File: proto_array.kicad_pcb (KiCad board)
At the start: 2 copper layers, 99.1 x 129.5 mm, 60 parts, among them P1 CONN_01X03, P2 CONN_01X03, P3 CONN_01X03, P4 CONN_01X03, P5 CONN_01X03, U1 ADS131E08, U2 BEAGLEBONEBLACK

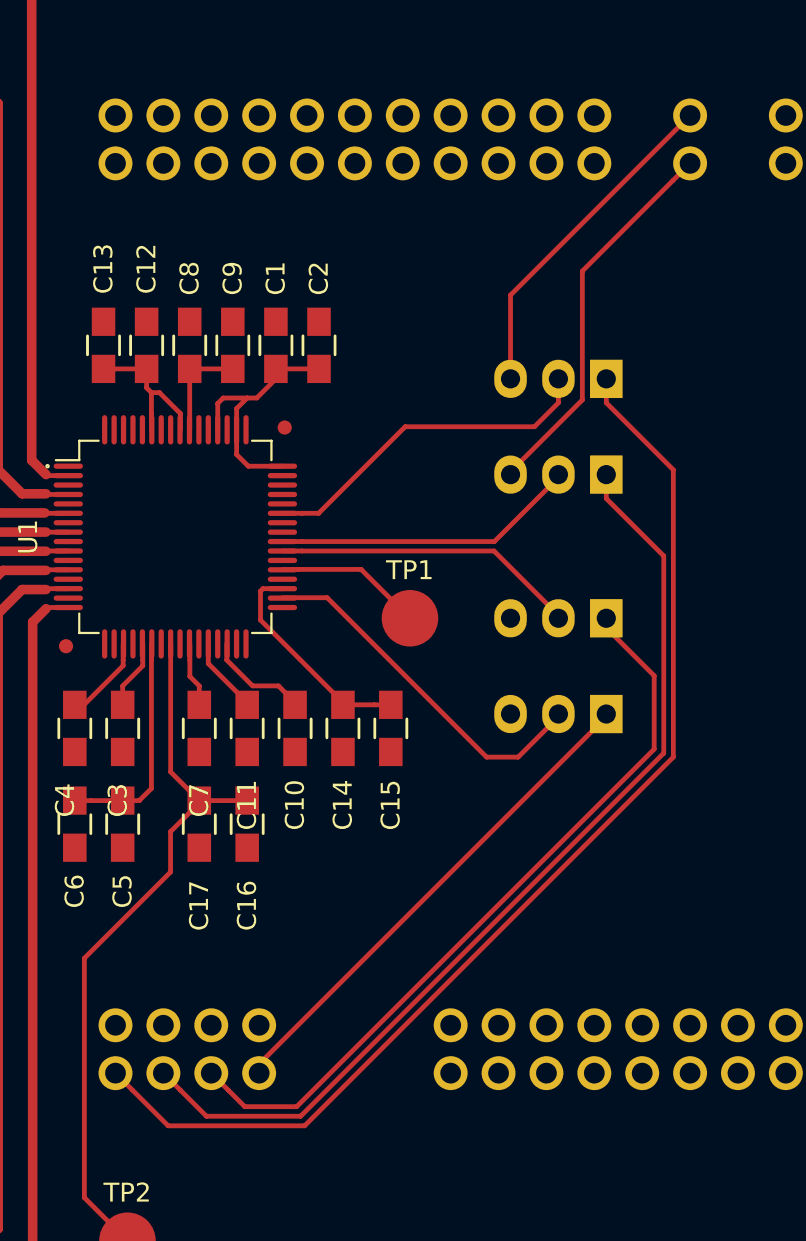
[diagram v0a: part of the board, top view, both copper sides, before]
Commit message: Eliminated the headers for SPI interface to make PCB single layer.
Signed-off-by: Chamon <[luizchamon@gmail.com>
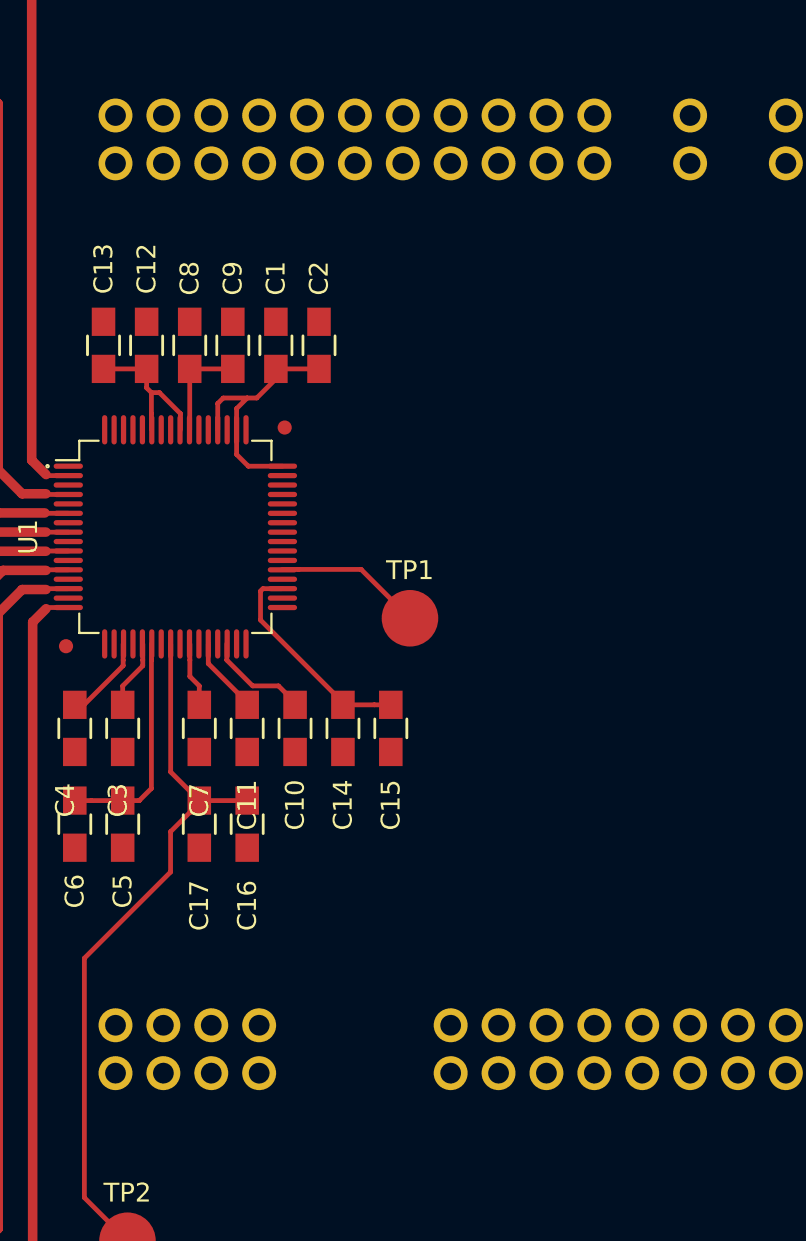
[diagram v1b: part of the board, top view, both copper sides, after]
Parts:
- removed P2, P3, P4, P5: CONN_01X03, Pin_Headers:Pin_Header_Straight_1x03
- moved P1 39.9 mm to (101.6, 49.5)
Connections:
- P1 pad 1: /PRU1_5 -> /BBB_VDD_5V
- P1 pad 2: Net-(P1-Pad2) -> AVDD
- P1 pad 3: /SPI0_CS -> /BBB_SYS_5V
- U1 pad 34: Net-(P3-Pad2) -> /PRU1_7
- U1 pad 39: Net-(P1-Pad2) -> /PRU1_5
- U1 pad 40: Net-(P2-Pad2) -> /PRU1_3
- U1 pad 43: Net-(P4-Pad2) -> /PRU1_1
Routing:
- net /PRU1_1: track 60.4 -> 0.00 mm
- net /PRU1_3: track 51.5 -> 0.00 mm
- net /PRU1_5: track 40.1 -> 0.00 mm
- net /PRU1_7: track 26.7 -> 0.48 mm
- net /SPI0_CLK: track 20.5 -> 0.00 mm
- net Net-(P3-Pad2): track 19.2 -> 0.00 mm
- net Net-(P4-Pad2): track 18.3 -> 0.00 mm
- net /SPI0_MISO: track 17.9 -> 0.00 mm
- net Net-(P1-Pad2): track 16.2 -> 0.00 mm
- net Net-(P2-Pad2): track 16.2 -> 0.00 mm

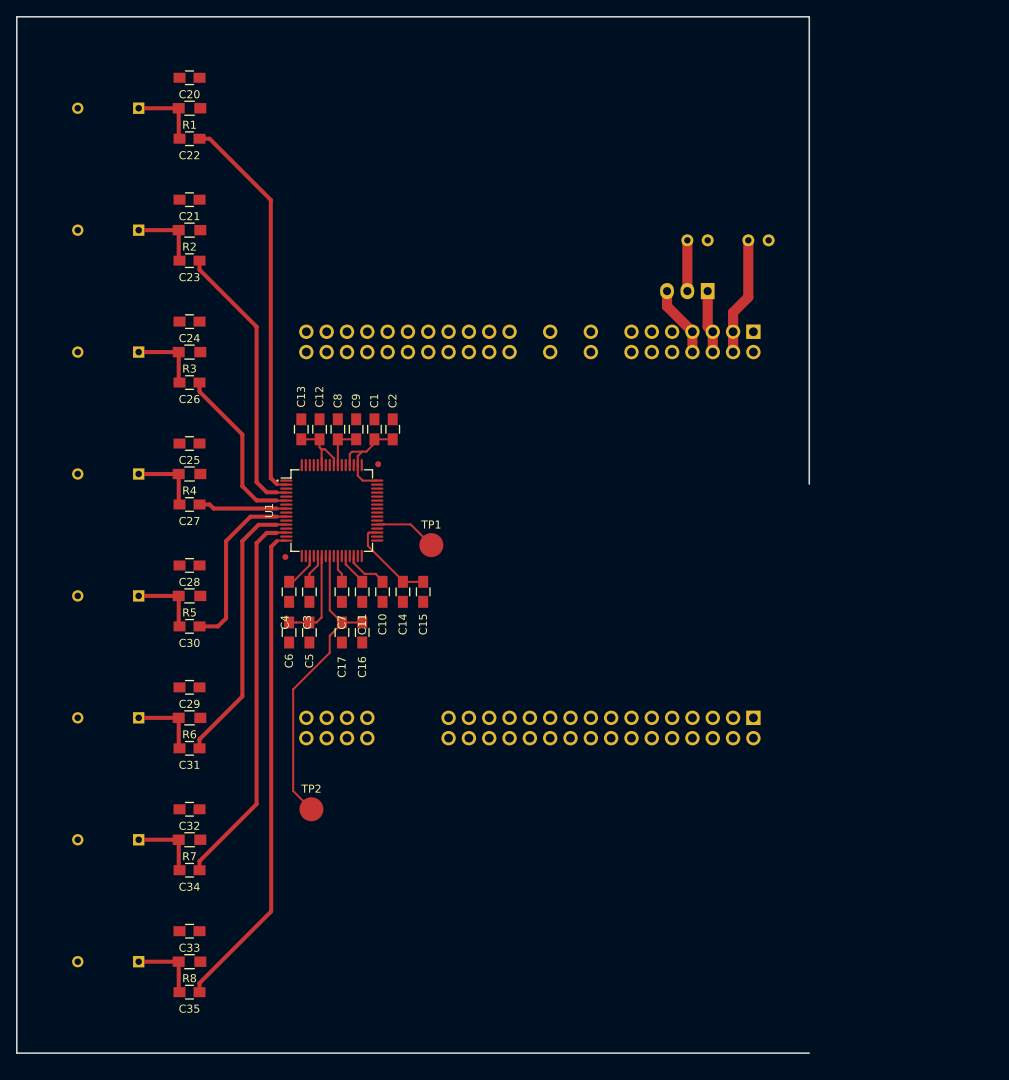
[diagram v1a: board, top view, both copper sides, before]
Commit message: Routed AVDD. Trying to solve ground routing.
Signed-off-by: Chamon <[luizchamon@gmail.com>
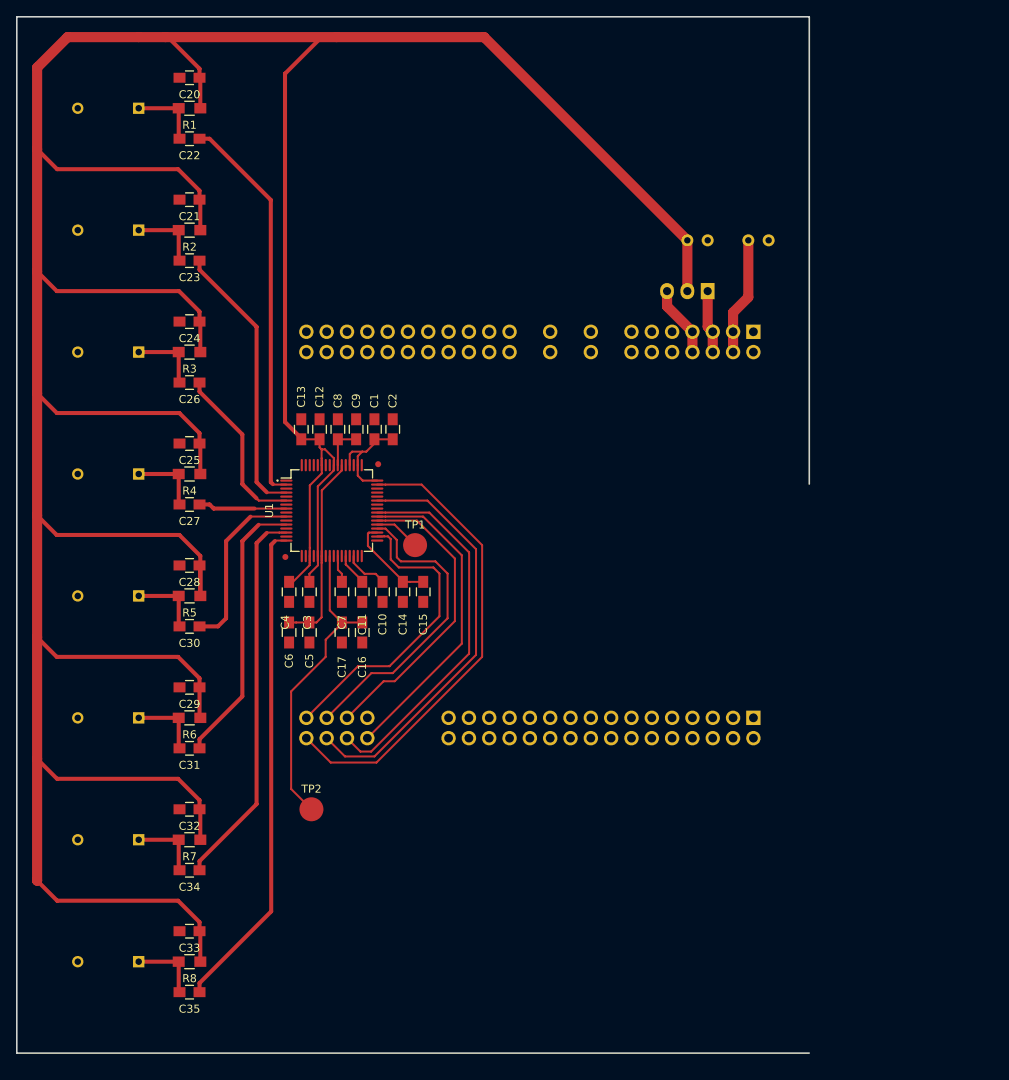
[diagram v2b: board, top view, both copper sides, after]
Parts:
- moved TP1 2.03 mm to (65.0, 81.3)
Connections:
- U1 pad 34: /PRU1_7 -> /PRU1_0
- U1 pad 36: /PRU1_4 -> /PRU1_2
- U1 pad 38: /PRU1_0 -> /PRU1_4
- U1 pad 39: /PRU1_5 -> /PRU1_7
- U1 pad 40: /PRU1_3 -> /PRU1_5
- U1 pad 43: /PRU1_1 -> /PRU1_3
- U1 pad 47: /PRU1_2 -> /PRU1_1
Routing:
- net AVDD: track 35.2 -> 528.6 mm
- net /PRU1_1: track 0.00 -> 58.9 mm
- net /PRU1_3: track 0.00 -> 53.0 mm
- net /PRU1_5: track 0.00 -> 47.2 mm
- net /PRU1_7: track 0.48 -> 40.3 mm
- net /PRU1_0: track 0.00 -> 38.4 mm
- net /PRU1_2: track 0.00 -> 38.3 mm
- net /PRU1_4: track 0.00 -> 38.0 mm
- net Net-(TP1-Pad1): track 7.84 -> 5.80 mm

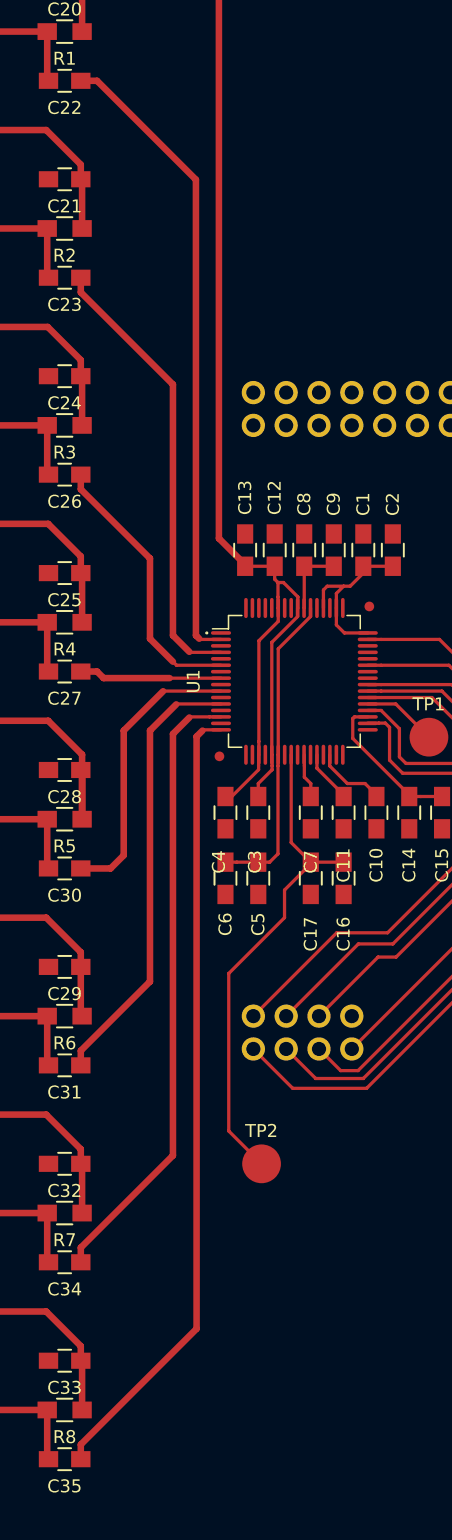
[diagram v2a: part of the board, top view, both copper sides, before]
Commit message: * Fix PRU connections on the schematic * Reduce microphone tracks to fit ground plane * Remove fiducials from ADC IC
Signed-off-by: Chamon <[luizchamon@gmail.com>
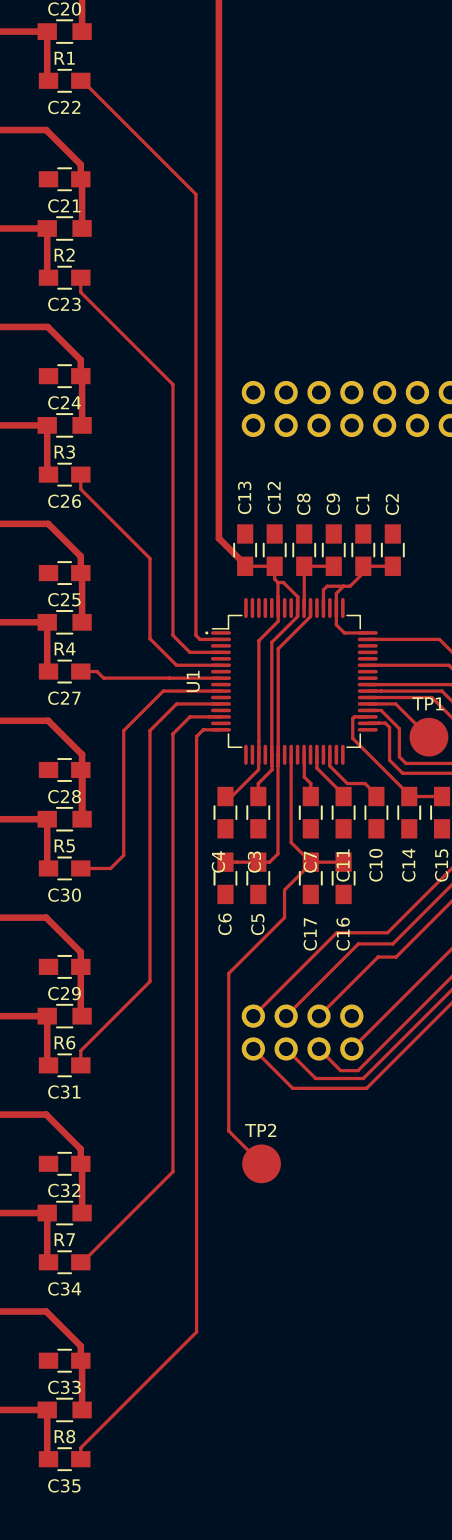
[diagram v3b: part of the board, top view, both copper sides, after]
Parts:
- U1: footprint micarray:LQFP-64_12x12_Pitch0.5mm -> micarray:LQFP-64_12x12_Pitch0.5mm_NoFid
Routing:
- net /MIC_1: track 49.4 -> 48.8 mm

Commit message: Final PCB with one airwire.
Signed-off-by: Chamon <[luizchamon@gmail.com>
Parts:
- removed TP2: TESTPOINT, Measurement_Points:Measurement_Point_Round-SMD-Pad_Big
- moved C14 31.8 mm to (88.9, 68.1), turned to 90 degrees
- moved C15 31.7 mm to (91.4, 68.1), turned to 90 degrees
- moved C19 27.4 mm to (79.5, 47.0), turned to 180 degrees
- moved TP1 24.9 mm to (89.9, 81.8)
- moved C2 24.2 mm to (86.4, 68.1)
- moved C1 23.9 mm to (83.8, 68.1)
- moved C8 23.1 mm to (78.5, 66.8), turned to 180 degrees
- moved U2 22.9 mm to (106.7, 81.3)
- moved C11 22.9 mm to (81.3, 88.4)
- moved C16 22.9 mm to (81.3, 93.5)
- moved C18 22.9 mm to (121.9, 44.5)
- moved C20 22.9 mm to (59.7, 24.1)
- moved C21 22.9 mm to (59.7, 39.4)
- moved C22 22.9 mm to (59.7, 31.8)
- moved C23 22.9 mm to (59.7, 47.0)
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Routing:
- net DVDD: track 40.3 -> 110.3 mm
- net /VREFP: track 38.5 -> 11.5 mm
- net AGND: track 0.00 -> 21.7 mm
- net AVDD: track 528.6 -> 537.4 mm
- net /PRU1_4: track 38.0 -> 44.3 mm
- net /PRU1_0: track 38.4 -> 42.8 mm
- net /PRU1_7: track 40.3 -> 44.7 mm
- net /PRU1_2: track 38.3 -> 42.5 mm
- net /PRU1_5: track 47.2 -> 50.5 mm
- net /PRU1_3: track 53.0 -> 56.2 mm
- net /PRU1_1: track 58.9 -> 62.1 mm
- net Net-(TP1-Pad1): track 5.80 -> 7.52 mm
- net Net-(C8-Pad1): track 5.52 -> 6.47 mm
- added copper zone on F.Cu, net AGND
- added copper zone on F.Cu, net DVDD
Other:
- board text added: "An airwire is required between the digital ground pours."

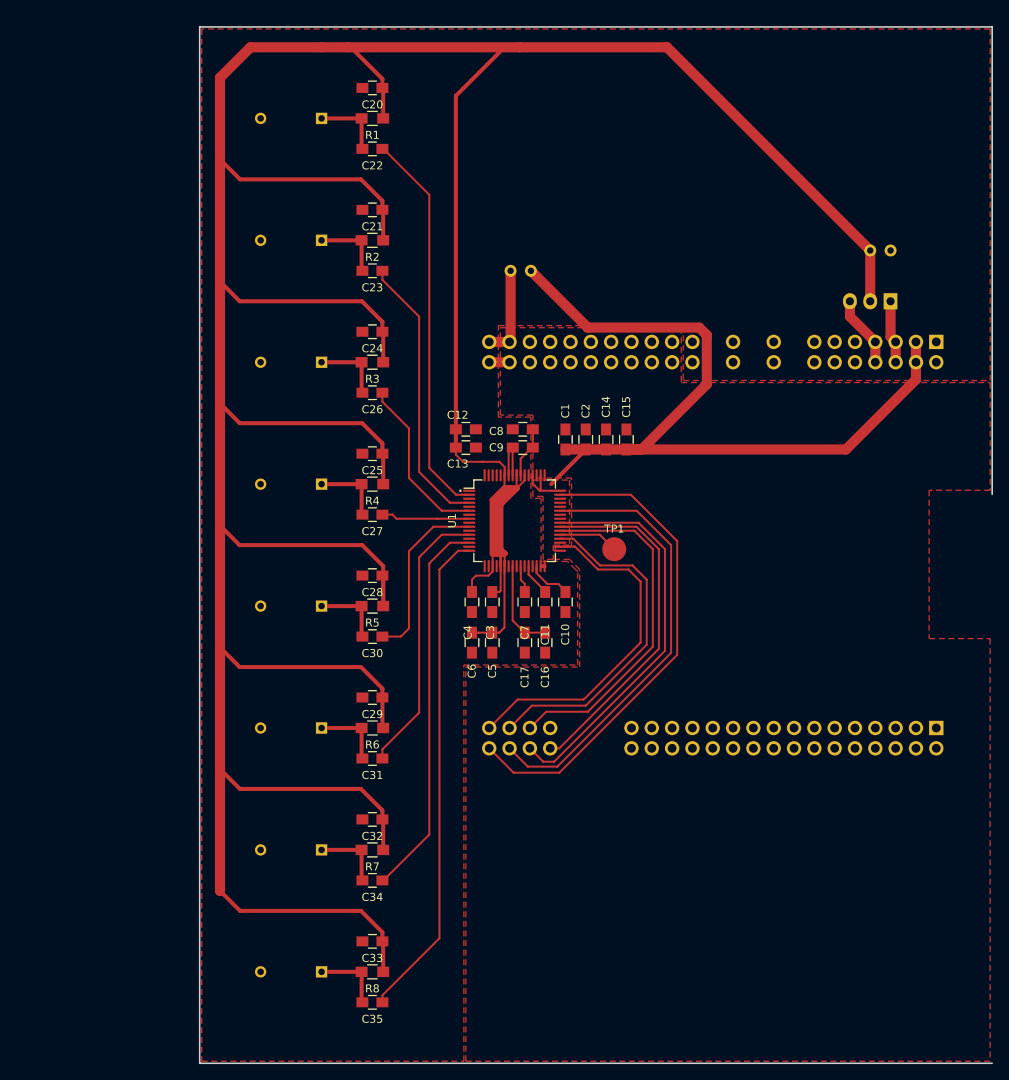
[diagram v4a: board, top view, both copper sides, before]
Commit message: * Add ADC footprint without fiducials * Remove unused pin headers from BBB * Modify eletret footprint
Signed-off-by: Chamon <[luizchamon@gmail.com>
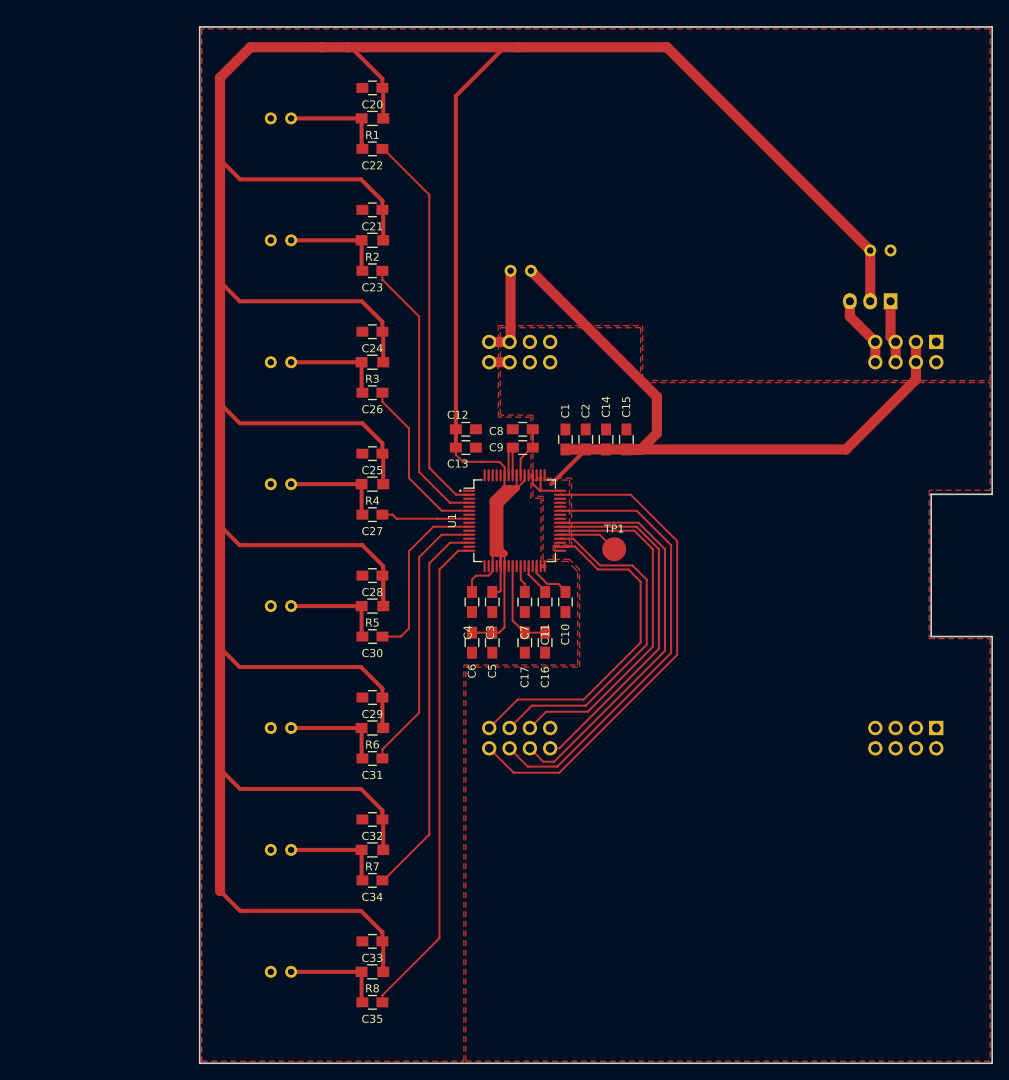
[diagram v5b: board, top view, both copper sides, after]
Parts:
- MIC1, MIC2, MIC3, MIC4, MIC5, MIC6, MIC7, MIC8: footprint Discret:BUZ3-5 -> Capacitors_Elko_ThroughHole:Elko_vert_20x10mm_RM2.5_CopperClear
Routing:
- net DVDD: track 110.3 -> 98.8 mm
- net Net-(C35-Pad2): track 8.85 -> 12.7 mm
- net Net-(C34-Pad2): track 8.85 -> 12.7 mm
- net Net-(C31-Pad2): track 8.85 -> 12.7 mm
- net Net-(C30-Pad2): track 8.85 -> 12.7 mm
- net Net-(C27-Pad2): track 8.85 -> 12.7 mm
- net Net-(C26-Pad2): track 8.85 -> 12.7 mm
- net Net-(C23-Pad2): track 8.85 -> 12.7 mm
- net Net-(C22-Pad2): track 8.85 -> 12.7 mm
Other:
- outline, holes or cut-outs redrawn
